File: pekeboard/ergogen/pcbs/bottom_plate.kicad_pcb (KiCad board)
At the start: 2 copper layers, 150.9 x 124.7 mm, 0 parts

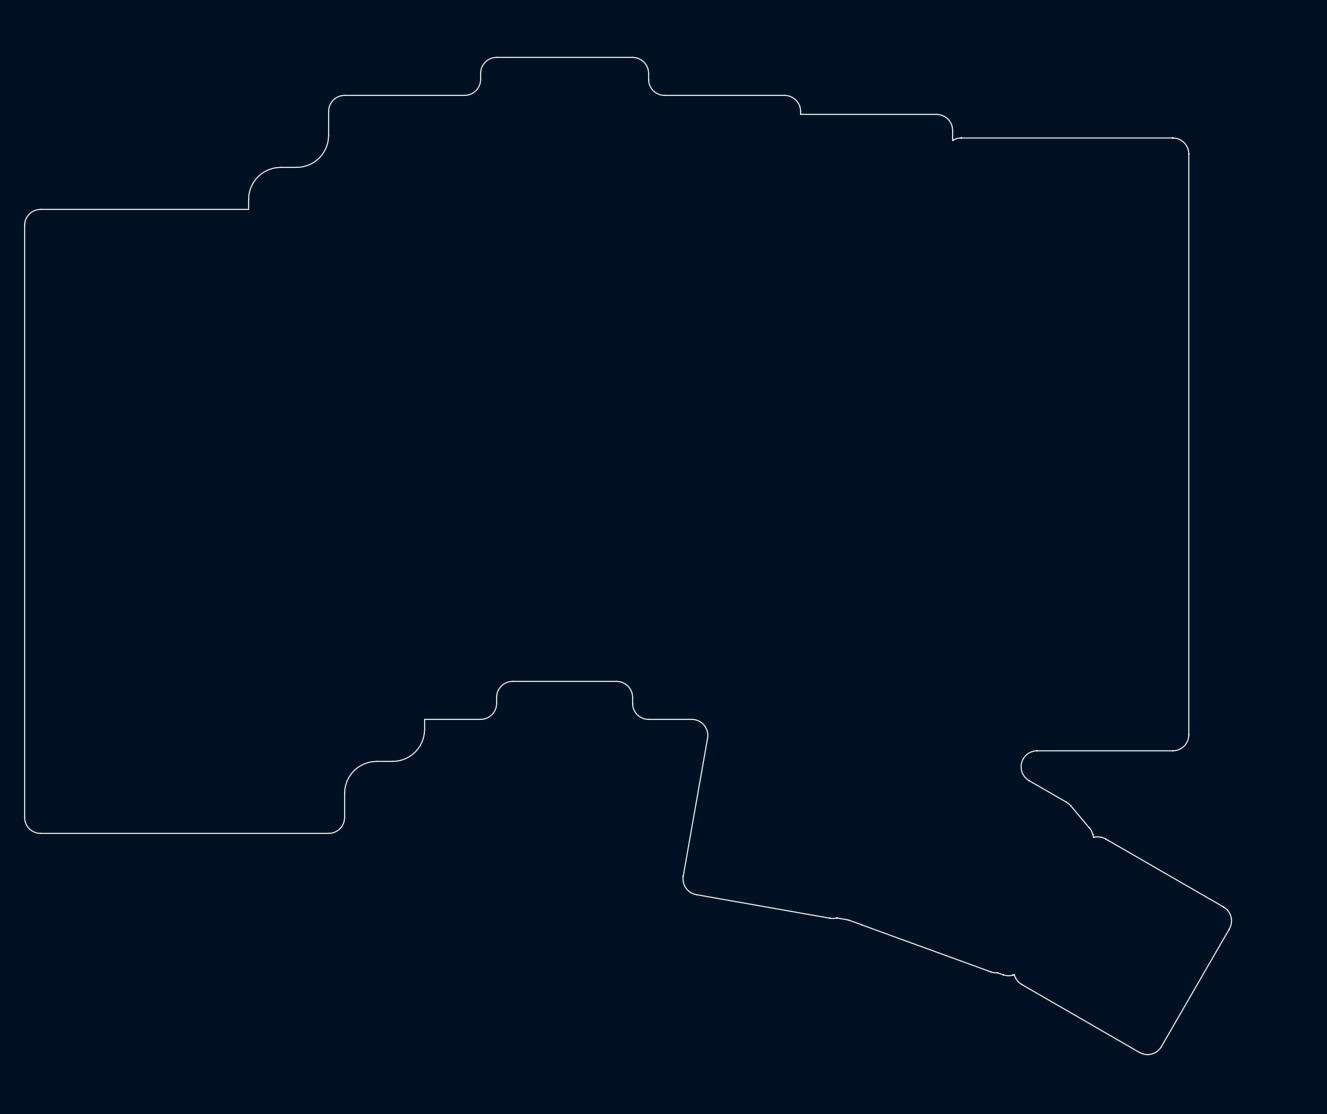
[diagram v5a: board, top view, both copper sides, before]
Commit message: Adjusting mounting holes
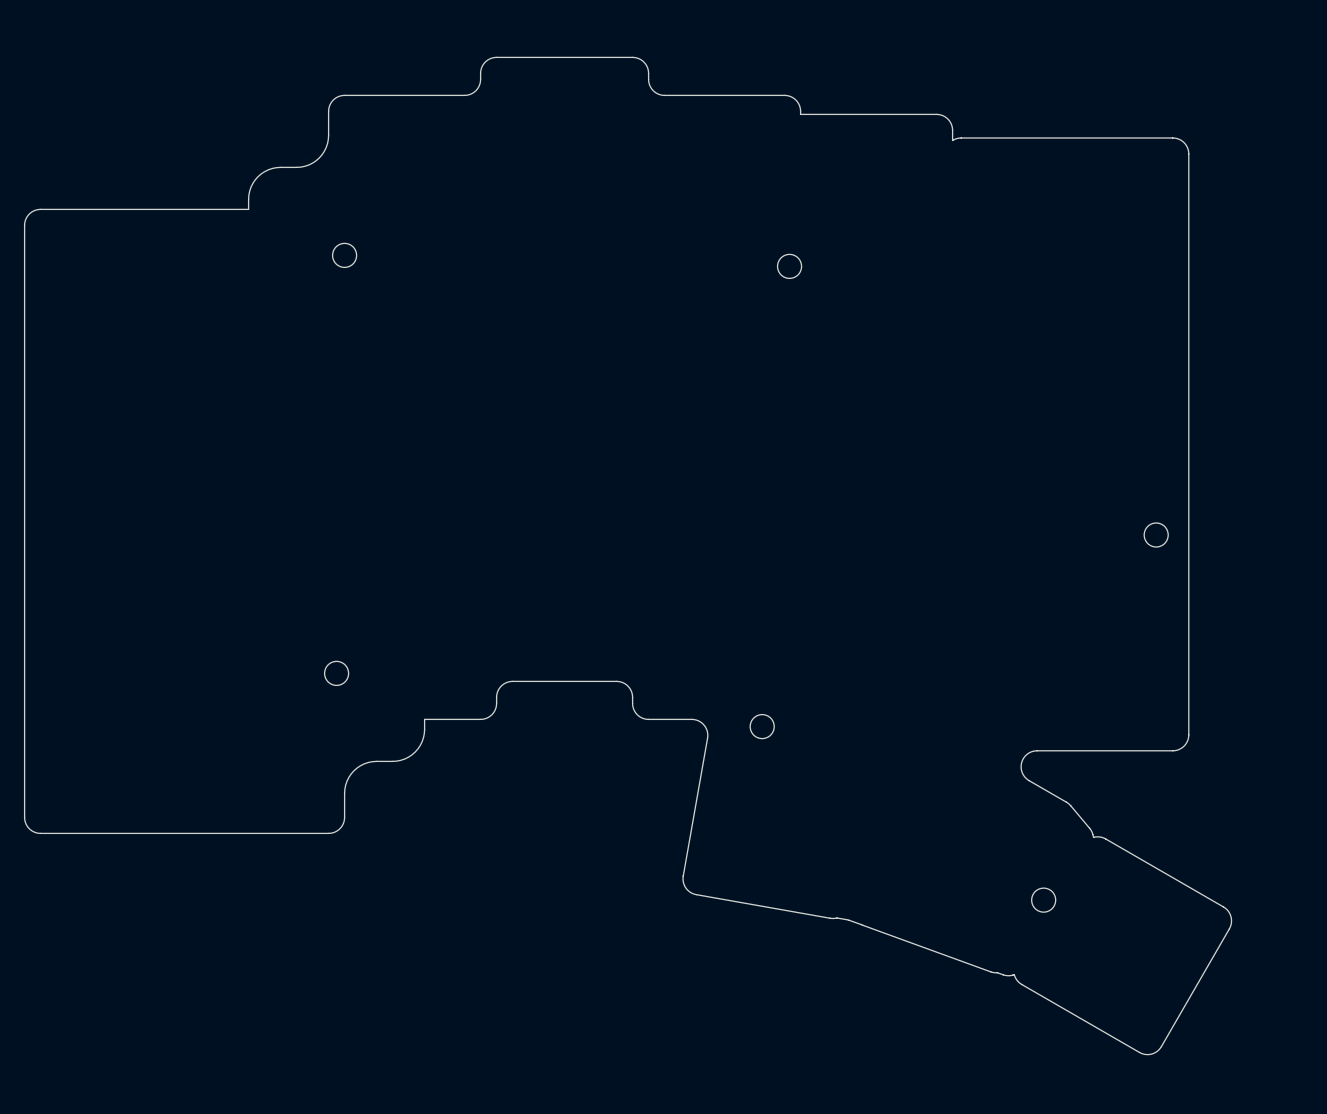
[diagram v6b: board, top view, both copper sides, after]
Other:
- outline, holes or cut-outs redrawn

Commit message: Fix mounting hole outside PCB
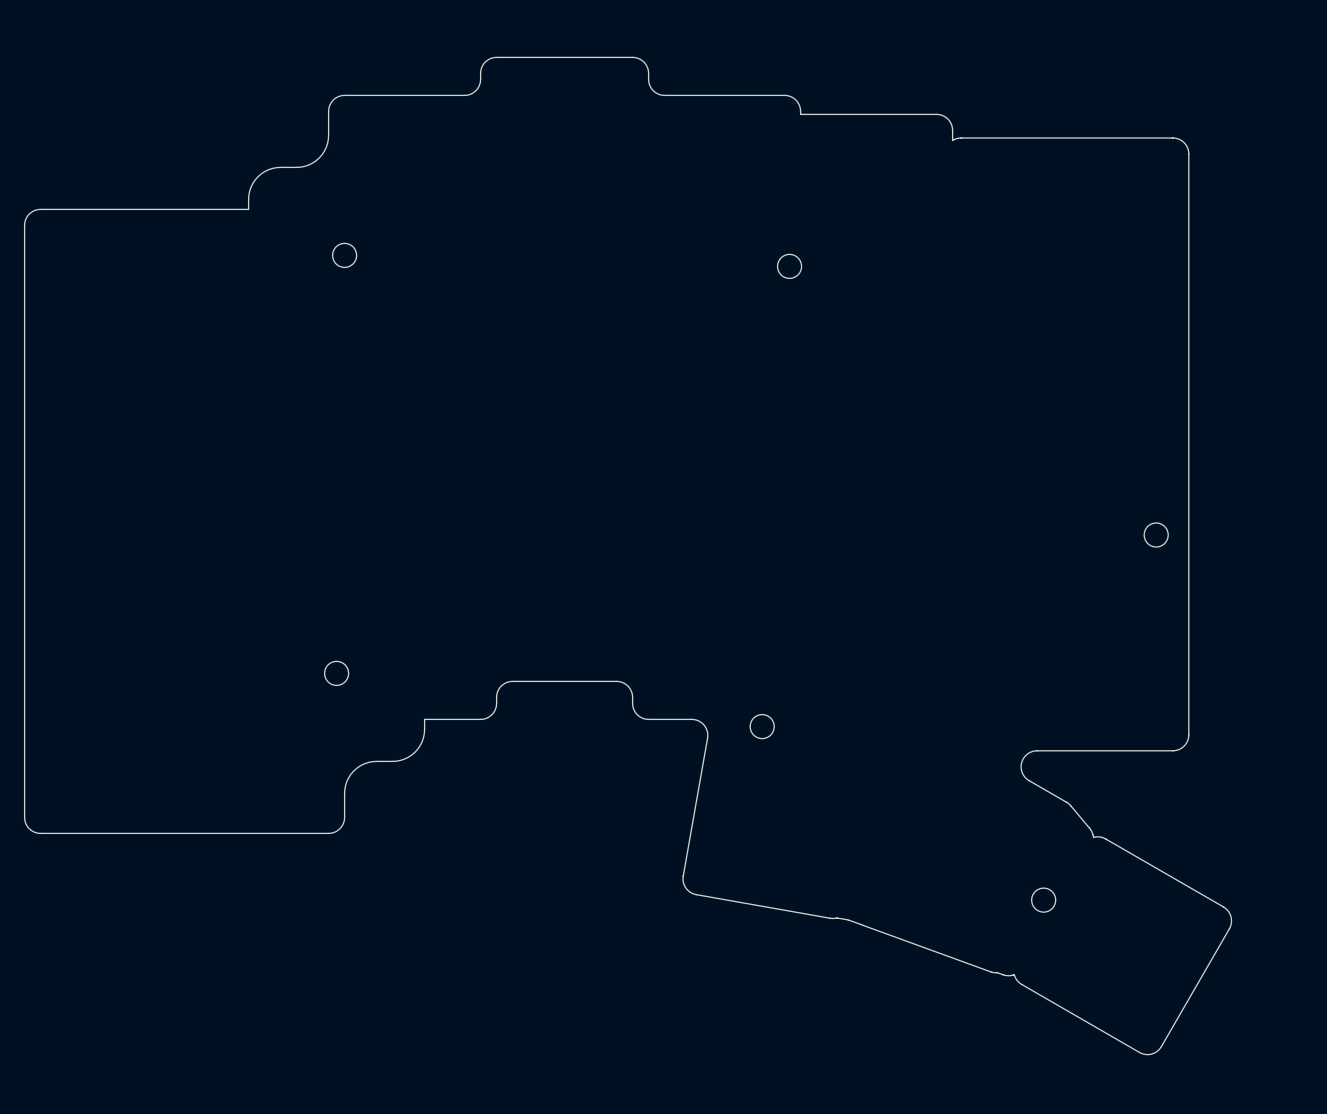
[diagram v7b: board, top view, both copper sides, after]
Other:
- outline, holes or cut-outs redrawn

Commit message: reversible diodes removing fill zone
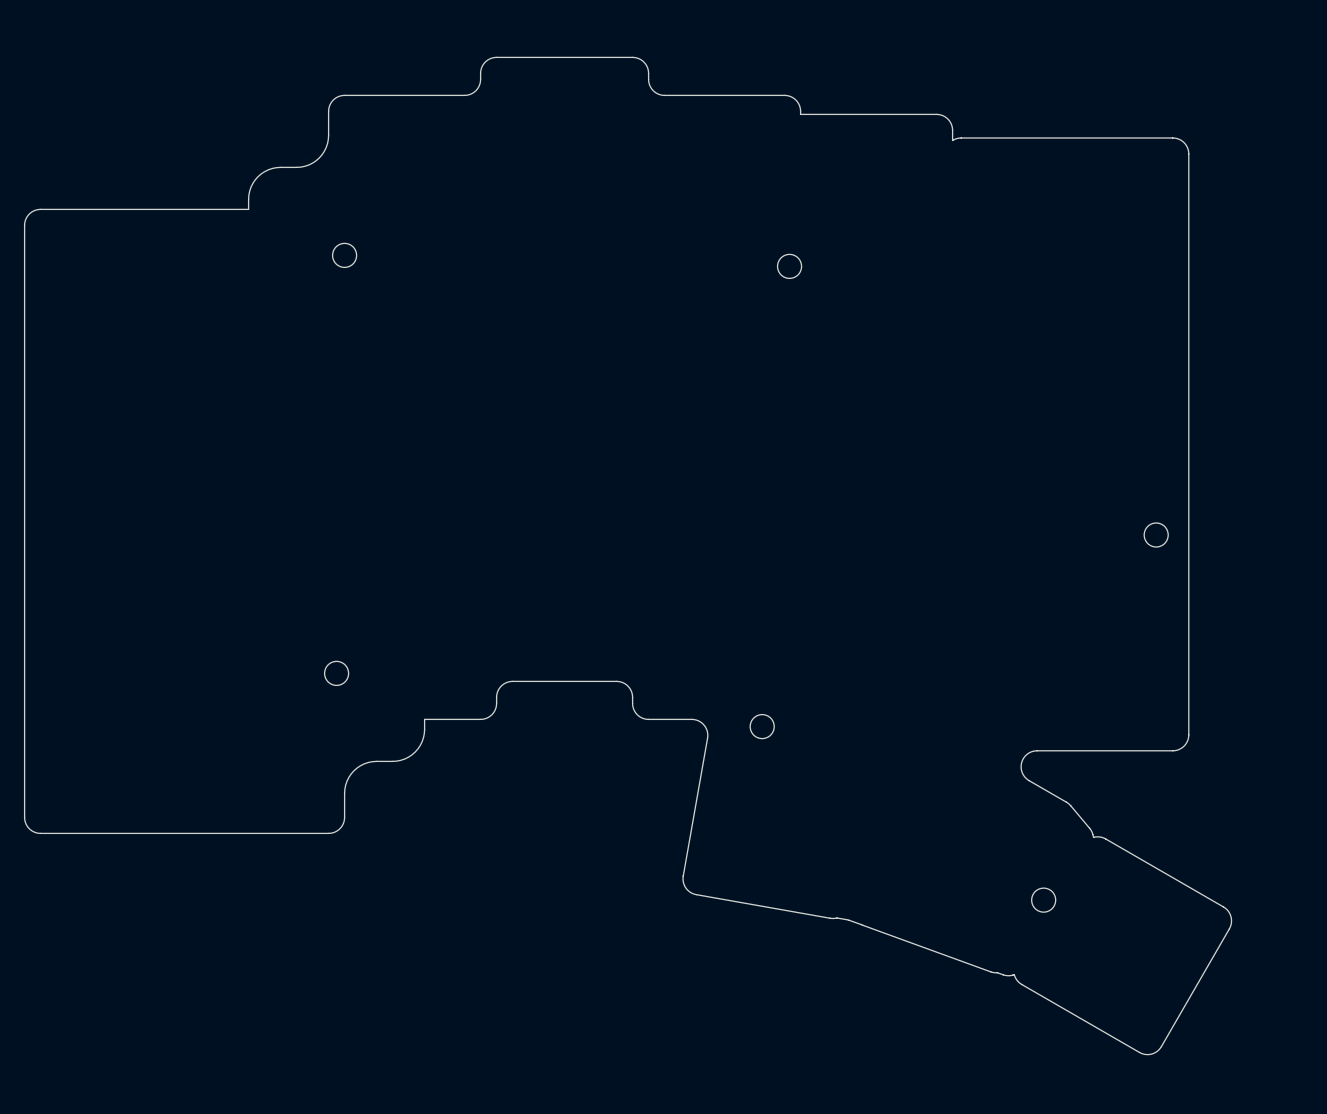
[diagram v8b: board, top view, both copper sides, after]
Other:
- outline, holes or cut-outs redrawn
